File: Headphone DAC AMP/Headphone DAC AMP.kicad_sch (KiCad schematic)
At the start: 0 parts

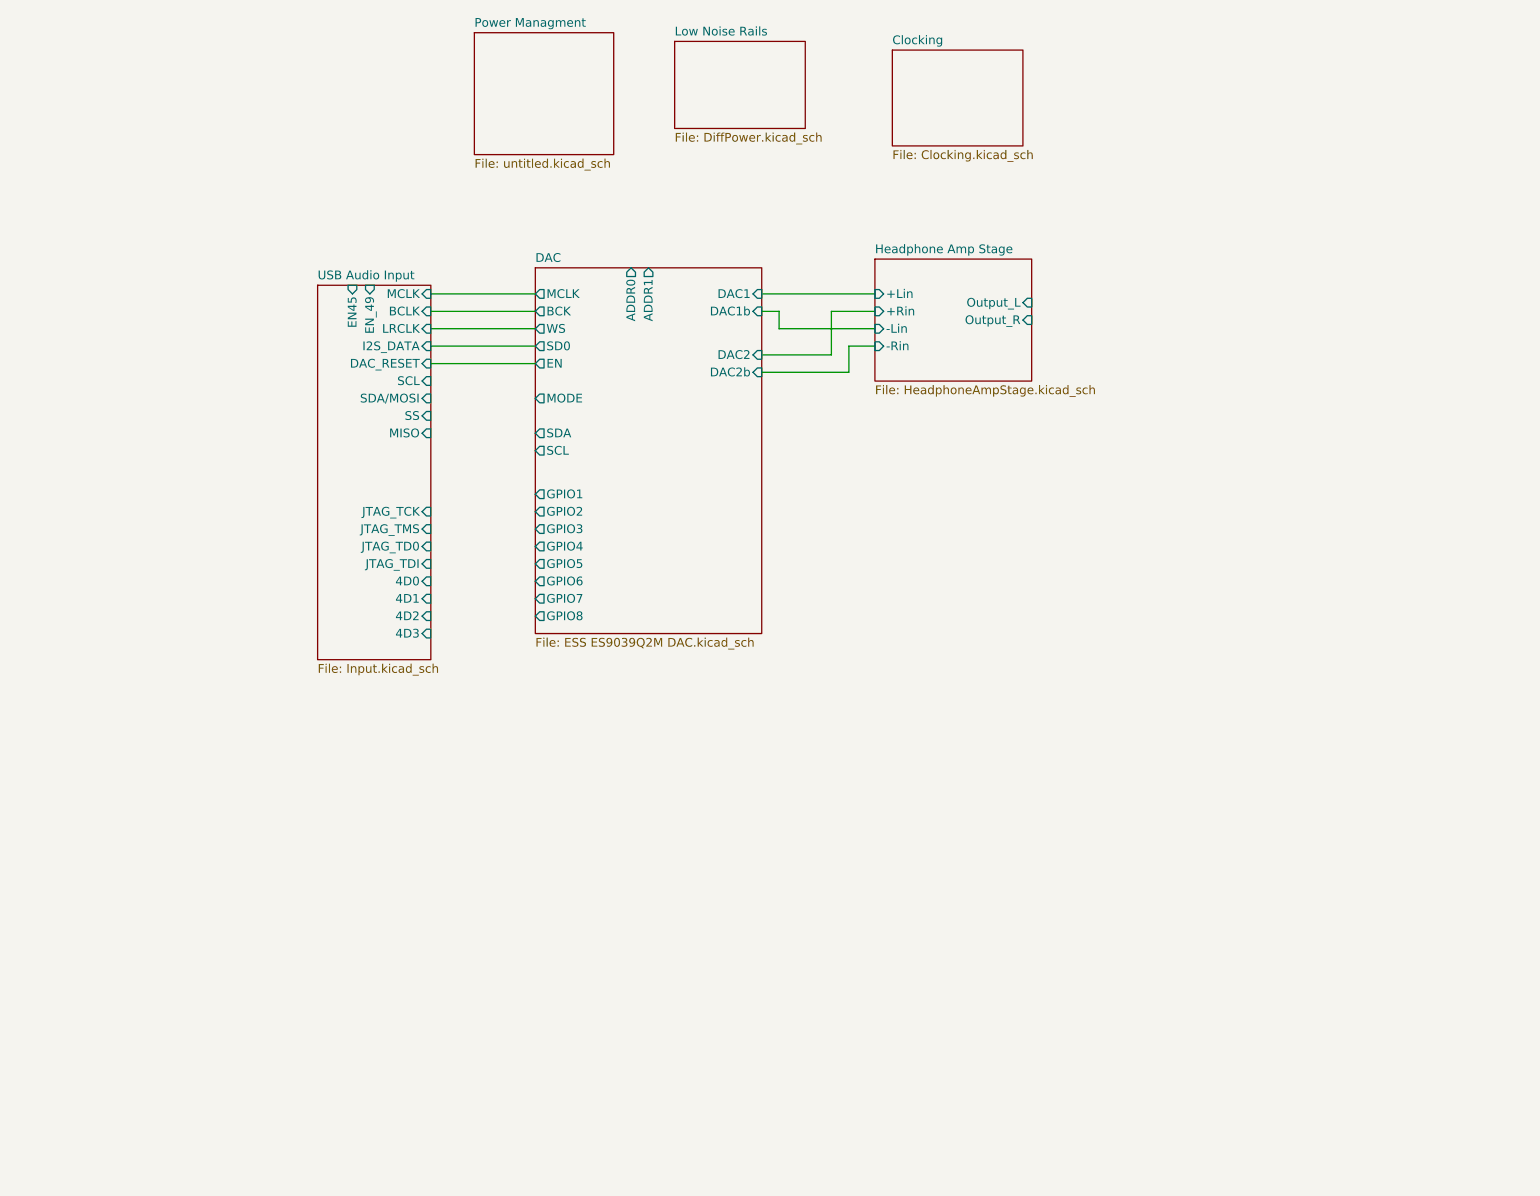
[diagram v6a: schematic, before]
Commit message: Completed a significant amount of the power and routing
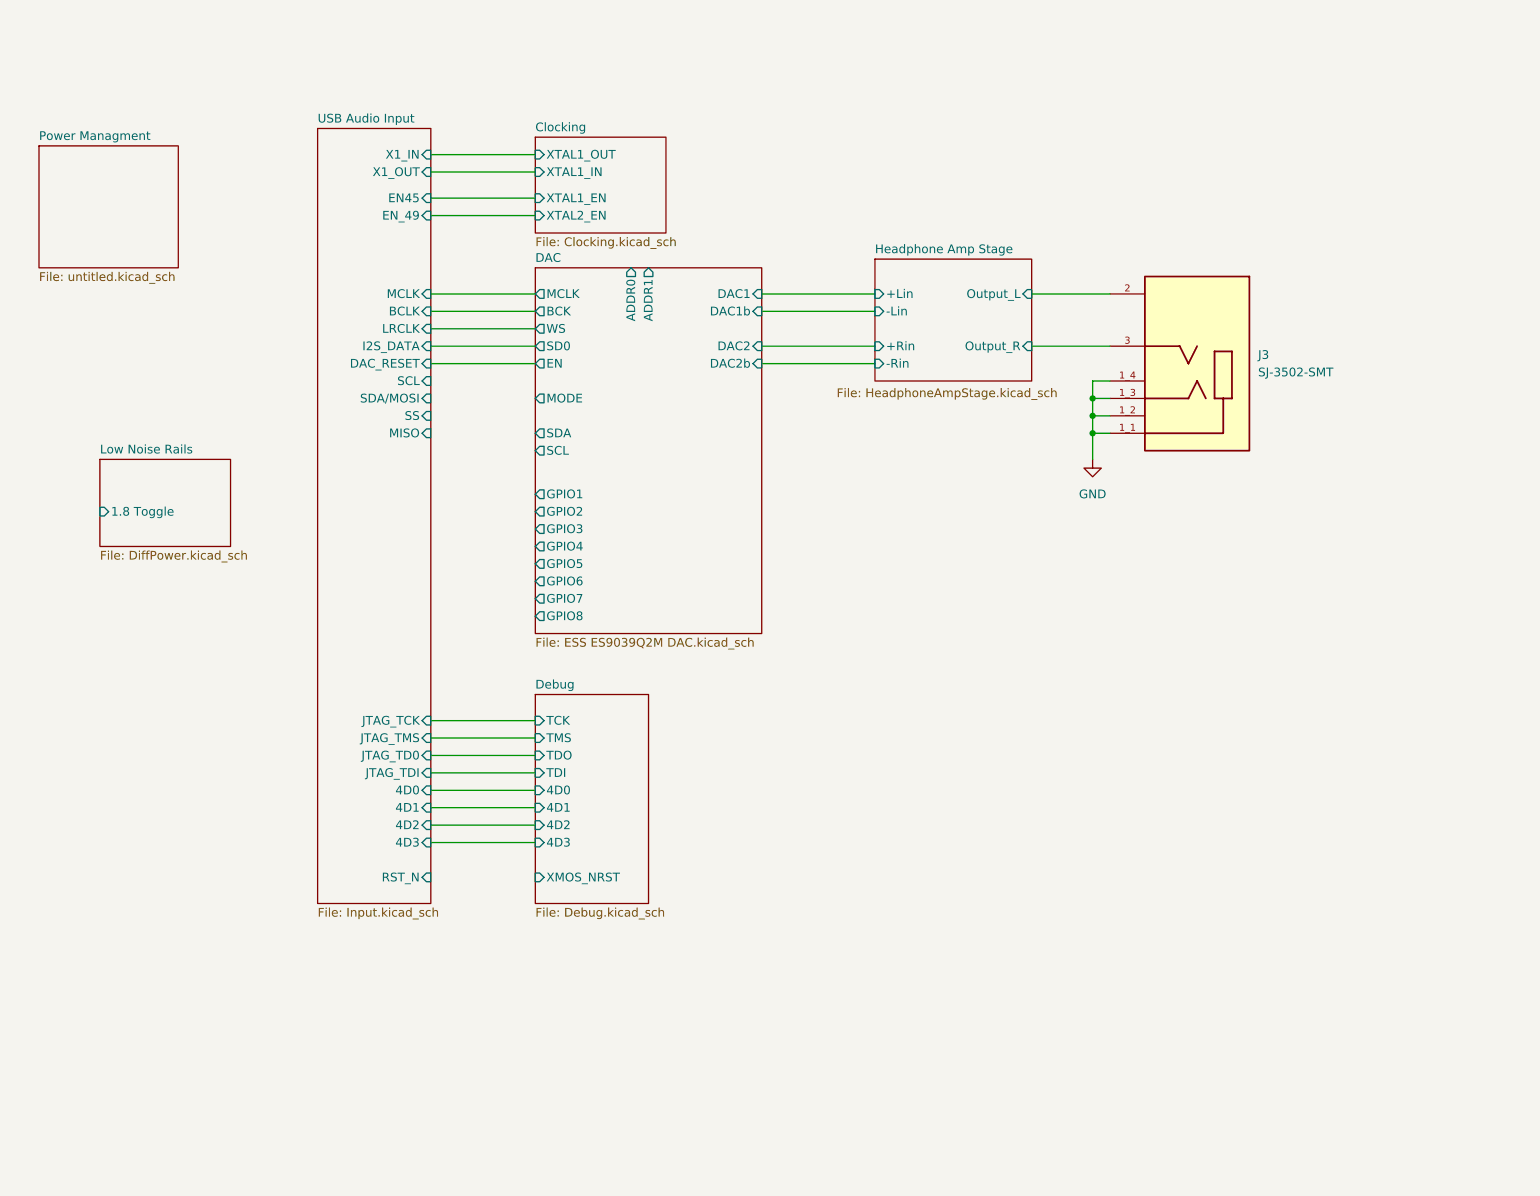
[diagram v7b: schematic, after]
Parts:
- added J3: SJ-3502-SMT, SJ-3502-SMT:CUI_SJ-3502-SMT, symbol SJ-3502-SMT:SJ-3502-SMT
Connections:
- net Headphone Amp Stage/Output_L: now also J3.2
- net Headphone Amp Stage/Output_R: now also J3.3
- new net GND: J3.1_1, J3.1_2, J3.1_3, J3.1_4
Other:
- added sheet Debug (Debug.kicad_sch)
- sheet Clocking ports: added XTAL1_EN, XTAL1_IN, XTAL1_OUT, XTAL2_EN; removed none
- sheet Low Noise Rails ports: added 1.8 Toggle; removed none
- sheet USB Audio Input ports: added RST_N, X1_IN, X1_OUT; removed none

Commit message: Added ground and 0.9v
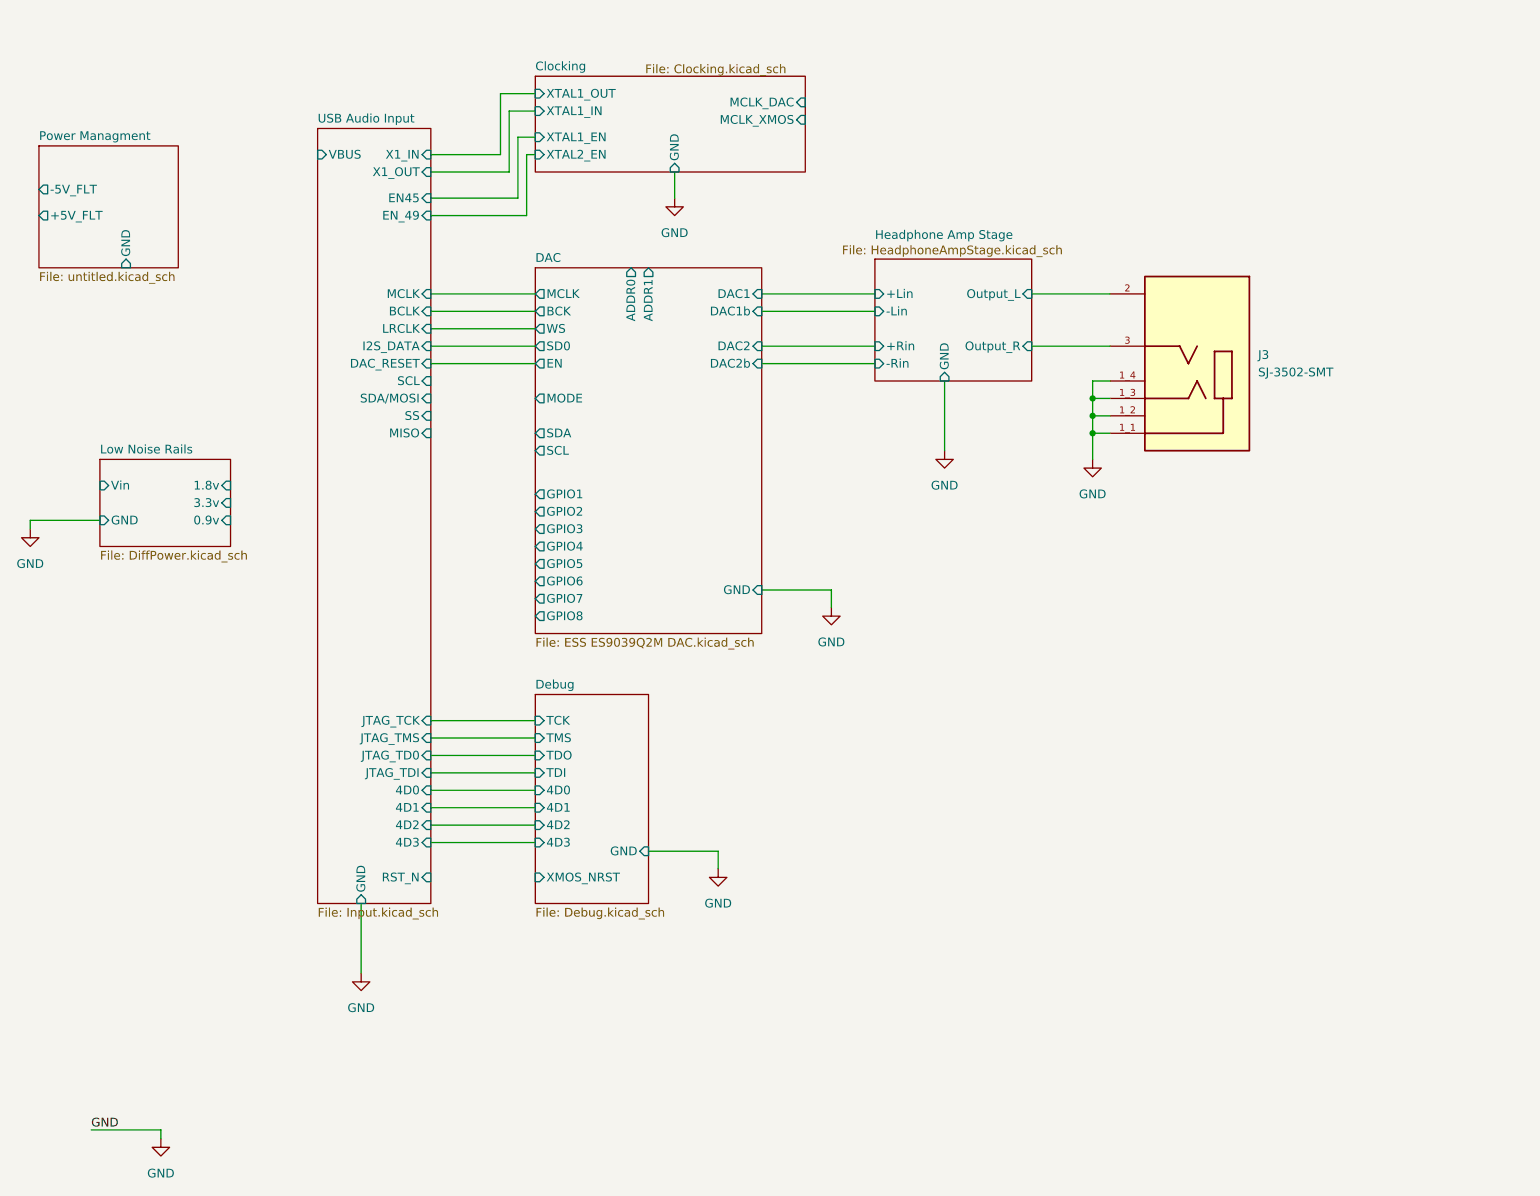
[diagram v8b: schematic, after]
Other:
- sheet Clocking ports: added GND, MCLK_DAC, MCLK_XMOS; removed none
- sheet DAC ports: added GND; removed none
- sheet Debug ports: added GND; removed none
- sheet Headphone Amp Stage ports: added GND; removed none
- sheet Low Noise Rails ports: added 0.9v, 1.8v, 3.3v, GND, Vin; removed 1.8 Toggle
- sheet Power Managment ports: added +5V_FLT, -5V_FLT, GND; removed none
- sheet USB Audio Input ports: added GND, VBUS; removed none
